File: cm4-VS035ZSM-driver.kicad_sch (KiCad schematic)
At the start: 4 parts, among them U101 USB-TYPE-C-018

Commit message: essential routing done
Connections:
- net +5V: now also Module101.77 (+5v_(Input)), Module101.79 (+5v_(Input)), Module101.81 (+5v_(Input)), Module101.83 (+5v_(Input)), Module101.85 (+5v_(Input)), Module101.87 (+5v_(Input))
- net GND: now also Module101.1 (GND), Module101.13 (GND), Module101.14 (GND), Module101.2 (GND), Module101.22 (GND), Module101.23 (GND), Module101.32 (GND), Module101.33 (GND), Module101.42 (GND), Module101.43 (GND), Module101.52 (GND), Module101.53 (GND), Module101.59 (GND), Module101.60 (GND), Module101.65 (GND), Module101.66 (GND), Module101.7 (GND), Module101.71 (GND), Module101.74 (GND), Module101.8 (GND), Module101.98 (GND)
- net +3V3: now reaches Module101.84 (+3.3v_(Output))
- net +3V3: now also Module101.86 (+3.3v_(Output))
- net +1V8: now reaches Module101.88 (+1.8v_(Output))
- net +1V8: now also Module101.90 (+1.8v_(Output))
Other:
- moved on the sheet: R101, R102, U101

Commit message: more routing
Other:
- moved on the sheet: R101, R102, U101

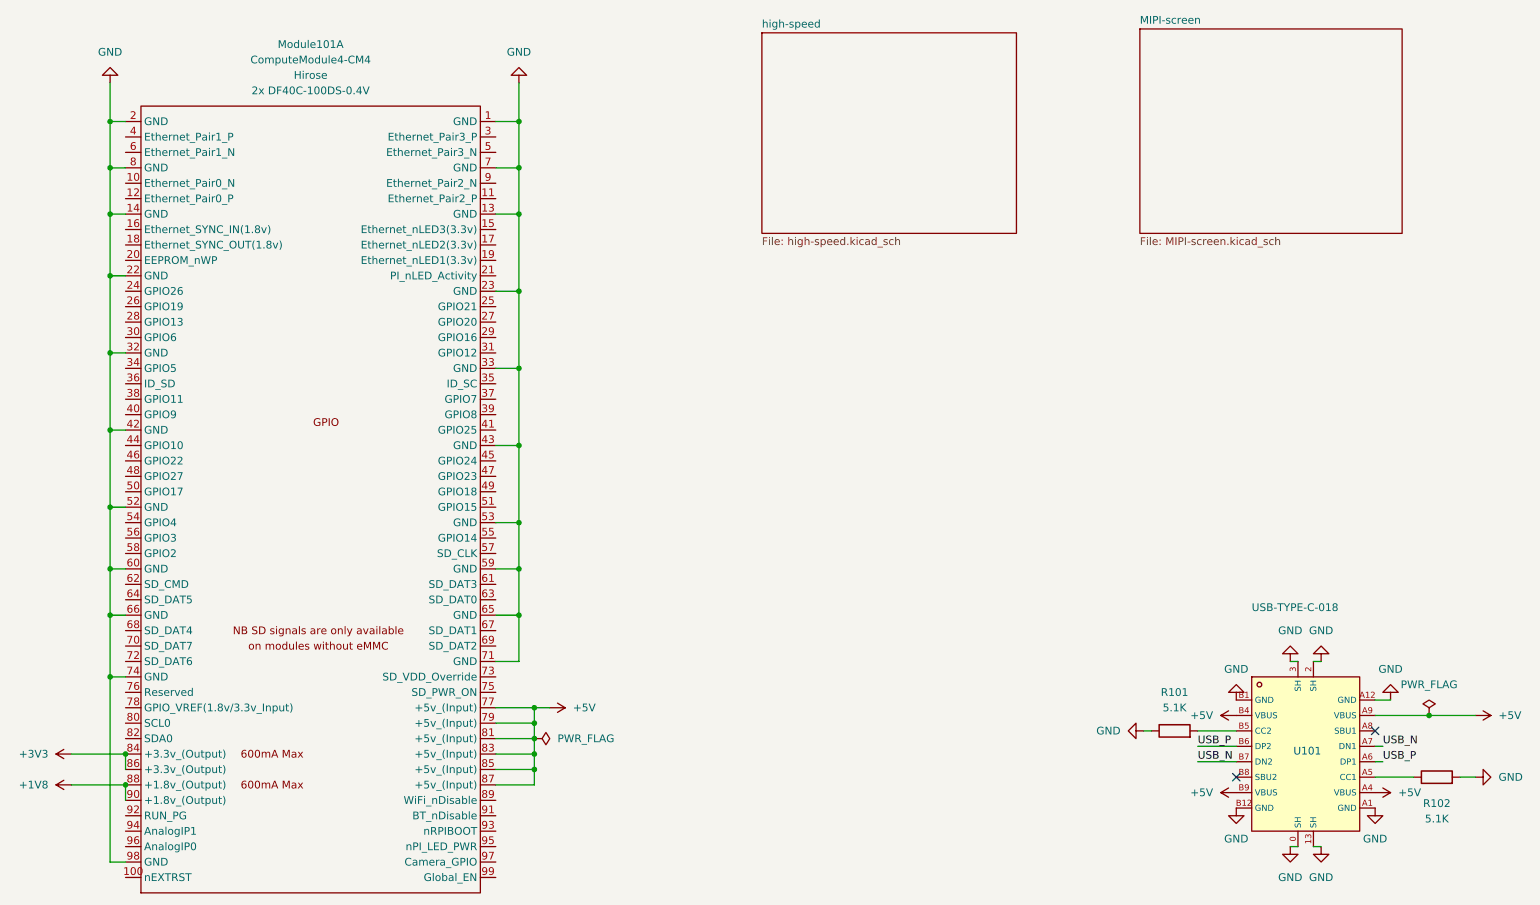
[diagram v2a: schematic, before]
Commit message: 1v8 buck and 4.7uh inductor
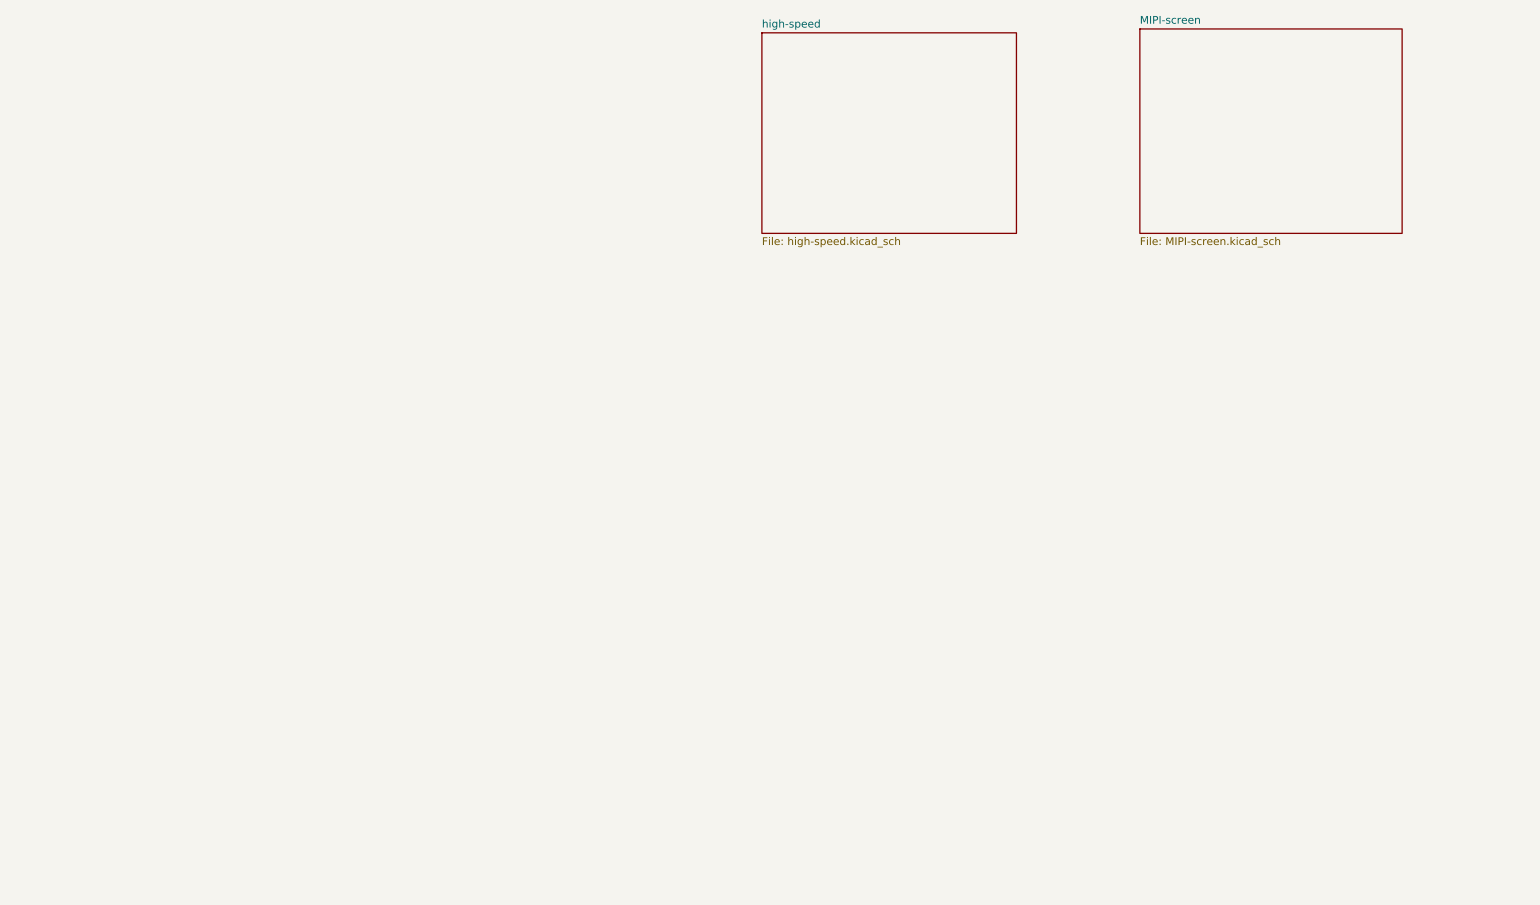
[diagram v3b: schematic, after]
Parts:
- removed Module101: ComputeModule4-CM4, CM4IO:Raspberry-Pi-4-Compute-Module, symbol CM4IO:ComputeModule4-CM4
- removed R101, R102: 5.1K, Resistor_SMD:R_0402_1005Metric, symbol Device:R
- removed U101: USB-TYPE-C-018, footprint:USB-C_SMD-TYPE-C-31-M-12, symbol USB-TYPE-C-018:USB-TYPE-C-018
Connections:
- no-connect marks 2 -> 0

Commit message: init layout
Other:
- added sheet References (references.kicad_sch)
- sheet MIPI-screen ports: added {LED_PWR}; removed none
- sheet high-speed ports: added {LED_PWR}; removed none
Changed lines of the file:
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@@
 	(generator_version "9.0")
 	(paper "A4")
+	(bus
+		(pts
+			(xy 210.82 35.56) (xy 214.63 35.56)
+		)
+		(stroke
+			(width 0)
+			(type default)
+		)
+	)
 	(sheet
-		(at 151.765 22.225)
-		(size 41.91 33.02)
+		(at 168.91 21.59)
+		(size 41.91 20.574)
 		(exclude_from_sim no)
 		(in_bom yes)
@@
 		)
 		(property "Sheetname" "high-speed"
-			(at 151.765 21.5134 0)
+			(at 168.91 20.8784 0)
 			(effects
 				(font
@@
 		)
 		(property "Sheetfile" "high-speed.kicad_sch"
-			(at 151.765 55.8296 0)
+			(at 168.91 42.7486 0)
 			(effects
 				(font
@@
 				)
 				(justify left top)
+			)
+		)
+		(pin "{LED_PWR}" input
+			(at 210.82 35.56 0)
+			(effects
+				(font
+					(size 1.27 1.27)
+				)
+				(justify right)
 			)
 		)
@@
 	)
 	(sheet
-		(at 213.995 21.59)
-		(size 43.18 33.655)
+		(at 213.36 62.23)
+		(size 44.45 38.1)
+		(exclude_from_sim no)
+		(in_bom yes)
+		(on_board yes)
+		(dnp no)
+		(fields_autoplaced yes)
+		(stroke
+			(width 0.1524)
+			(type solid)
+		)
+		(fill
+			(color 0 0 0 0.0000)
+		)
+		(property "Sheetname" "References"
+			(at 213.36 61.5184 0)
+			(effects
+				(font
+					(size 1.27 1.27)
+				)
+				(justify left bottom)
+			)
+		)
+		(property "Sheetfile" "references.kicad_sch"
+			(at 213.36 100.9146 0)
+			(effects
+				(font
+					(size 1.27 1.27)
+				)
+				(justify left top)
+			)
+		)
+		(instances
+			(project "cm4-VS035ZSM-driver"
+				(path "/9e206693-3fee-4fd4-91e0-40fbbe689518"
+					(page "4")
+				)
+			)
+		)
+	)
+	(sheet
+		(at 214.503 21.971)
+		(size 26.543 20.193)
 		(exclude_from_sim no)
 		(in_bom yes)
@@
 		)
 		(property "Sheetname" "MIPI-screen"
-			(at 213.995 20.8784 0)
+			(at 214.503 21.2594 0)
 			(effects
 				(font
@@
 		)
 		(property "Sheetfile" "MIPI-screen.kicad_sch"
-			(at 213.995 55.8296 0)
+			(at 214.503 42.7486 0)
 			(effects
 				(font
@@
 			)
 		)
+		(pin "{LED_PWR}" input
+			(at 214.503 35.56 180)
+			(effects
+				(font
+					(size 1.27 1.27)
+				)
+				(justify left)
+			)
+		)

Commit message: ok imma try kicad 10
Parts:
- added C212, C214, C220, C221, C222, C223: 4.7uF/16V, Capacitor_SMD:C_0603_1608Metric, symbol Device:C
- added C213, C215: 2.2uF/50V, Capacitor_SMD:C_0805_2012Metric, symbol Device:C
- added C216: 10uF/25V, Capacitor_SMD:C_0603_1608Metric, symbol Device:C
- added D403: B5817WS_C7420329, footprints:SOD-323_L1.7-W1.3-LS2.5-FD, symbol B5817WS_C7420329:B5817WS_C7420329
- added H1, H2, H3: MountingHole_Pad, MountingHole:MountingHole_3.2mm_M3_DIN965_Pad_TopBottom, symbol Mechanical:MountingHole_Pad
- added J1: Conn_01x22, footprints:CON22_1X22_DRB_XF2C_TYC, symbol XF2M-2215-1A:XF2M-2215-1A
- added J3: 245863050104829+, footprints:245863050104829_missing pads, symbol 245863050104829+:245863050104829+_missing_gnd
- added L204, L206, L207: 4.7uH, footprints:IND-SMD_L2.5-W2.0_SPH252012, symbol Device:L
- added R206: 5.1Ω/1%, Resistor_SMD:R_0805_2012Metric, symbol Device:R
- added R209: 100KΩ/1%, Resistor_SMD:R_0402_1005Metric, symbol Device:R
- added R3: 2.2kΩ, Resistor_SMD:R_0402_1005Metric, symbol Device:R
- added R4: 2.7kΩ, Resistor_SMD:R_0603_1608Metric, symbol Device:R
- added TP201: Test-1V8, TestPoint:TestPoint_THTPad_D2.0mm_Drill1.0mm, symbol Connector:TestPoint
- added U1: PZ254-2-08-WS, footprints:HDR-SMD_16P-P2.54-H-M-R2-C8-W12.0-N, symbol PZ254-2-08-WS:PZ254-2-08-WS
- added U2, U3: KF1027B-04P-G00-DFT-01B, footprints:SW-SMD_KF1027B-04P-G00-DFT-01B, symbol KF1027B-04P-G00-DFT-01B:KF1027B-04P-G00-DFT-01B
- added U202: TPS65132WRVCR_C2876379, footprints:WQFN-20_L4.0-W3.0-P0.50-BL-EP, symbol TPS65132WRVCR_C2876379:TPS65132WRVCR_C2876379
- added U203: LP3320B6F, footprints:SOT-23-6_L2.9-W1.6-P0.95-LS2.8-BL, symbol LP3320B6F:LP3320B6F
- added U204: MCP1603T-180I/OS, footprints:TSOT5_MC_MCH, symbol MCP1603T_180I_OS:MCP1603T-180I_OS
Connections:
- new net: L206.1, U204.5 (LX)
- new net: C222.1, U202.14 (REG), U202.18 (REG)
- new net: C213.1, U202.10 (CFLY2)
- new net: C213.2, U202.13 (CFLY1)
- new net: D403.1 (A), L204.2, U203.1 (LX)
- new net +1V8: J3.2, J3.4, J3.8, U3.4 (A4)
- new net +3V3: J1.22 (Pin_22), U1.10, U2.5 (B4), U2.6 (B3), U2.7 (B2), U2.8 (B1)
- new net +5V7: J3.3, U3.3 (A3)
- new net +5V7_EN: U1.6, U2.3 (A3), U202.5 (ENP)
- new net +5V7_OUT: C221.1, U202.15 (OUTP), U202.16 (OUTP), U3.6 (B3)
- new net +5V_IN: C214.2, C216.2, C223.1, L204.1, L207.1, U1.12, U202.4 (VIN), U203.6 (VIN), U204.1 (VIN)
- new net -5V7: J3.7, U3.2 (A2)
- new net -5V7_EN: U1.4, U2.2 (A2), U202.6 (ENN)
- new net -5V7_OUT: C220.1, U202.9 (OUTN), U3.7 (B2)
- new net 1V8_EN: U1.8, U2.4 (A4), U204.3 (*SHDN)
- new net 1V8_OUT: C212.1, L206.2, TP201.1, U204.4 (VFB/VOUT), U3.5 (B4)
- new net BL_DRV_EN: U1.2, U2.1 (A1)
- new net DSI0_CLK.N: J1.8 (Pin_8), J3.18
- new net DSI0_CLK.P: J1.9 (Pin_9), J3.20
- new net DSI0_DATA.0_N: J1.2 (Pin_2), J3.11
- new net DSI0_DATA.0_P: J1.3 (Pin_3), J3.13
- new net DSI0_DATA.1_N: J1.5 (Pin_5), J3.17
- new net DSI0_DATA.1_P: J1.6 (Pin_6), J3.19
- new net DSI0_DATA.2_N: J1.12 (Pin_12), J3.24
- new net DSI0_DATA.2_P: J1.11 (Pin_11), J3.26
- new net DSI0_DATA.3_N: J1.15 (Pin_15), J3.12
- new net DSI0_DATA.3_P: J1.14 (Pin_14), J3.14
- new net GND: C212.2, C214.1, C215.2, C216.1, C220.2, C221.2, C222.2, C223.2, H1.1, H2.1, H3.1, J1.1 (Pin_1), J1.10 (Pin_10), J1.13 (Pin_13), J1.16 (Pin_16), J1.19 (Pin_19), J1.23 (Pin_23_case), J1.24 (Pin_24_case), J1.4 (Pin_4), J1.7 (Pin_7), J3.1, J3.10, J3.15, J3.16, J3.21, J3.22, J3.27, J3.28, J3.33, J3.34, J3.39, J3.40, J3.43, J3.46, J3.49, J3.5, J3.50, J3.6, J3.9, J3.MP1, J3.MP2, J3.MP3, J3.MP4, J3.MP5, J3.MP6, R206.2, R209.2, R4.2, U202.1 (PGND), U202.11 (PGND), U202.12 (PGND), U202.17 (AGND), U202.2 (PGND), U202.21 (EP), U202.3 (AGND), U203.2 (GND), U204.2 (GND)
- new net LCD_CONNECTOR_PWM: J3.48, U1.5
- new net LCD_RESET_1V8: J3.42, R3.2, R4.1, U1.1
- new net LCD_RESET_3V3: J1.17 (Pin_17), R3.1, U1.3
- new net LED_PWM: J1.18 (Pin_18), R209.1, U1.9, U203.4 (EN)
- new net LED_PWR.A_IN: J3.41, U3.1 (A1)
- new net LED_PWR.A_OUT: C215.1, D403.2 (K), U1.14, U3.8 (B1)
- new net LED_PWR.K: J3.45, J3.47, R206.1, U1.16, U203.3 (FB)
- new net SCL_3V3: J1.20 (Pin_20), U1.13, U202.8 (SCL)
- new net SDA_3V3: J1.21 (Pin_21), U1.15, U202.7 (SDA)
- new net SW: L207.2, U202.19 (SW), U202.20 (SW)
- new net TE: J3.44, U1.11
- no-connect marks 0 -> 11
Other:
- removed sheet MIPI-screen
- removed sheet References
- removed sheet high-speed
- note added: "1V8 Buck"
- note added: "Broken out for testing"
- note added: "Display Mezzanine"
- note added: "Interfacing"
- note added: "LCD Bias"
- note added: "LED driver"
- note added: "LED goes between here FB is used to sense drop in voltage"
- note added: "Need 5V input, all the chips does accept 5v in"
- note added: "PWM controlled"
- note added: "Pi ribbon cable"
- note added: "Positive 5.7V and negative 5.7V"
- note added: "input"
- note added: "manual enable for power"
- note added: "manual voltage rail control (off by default)"
- note added: "output"

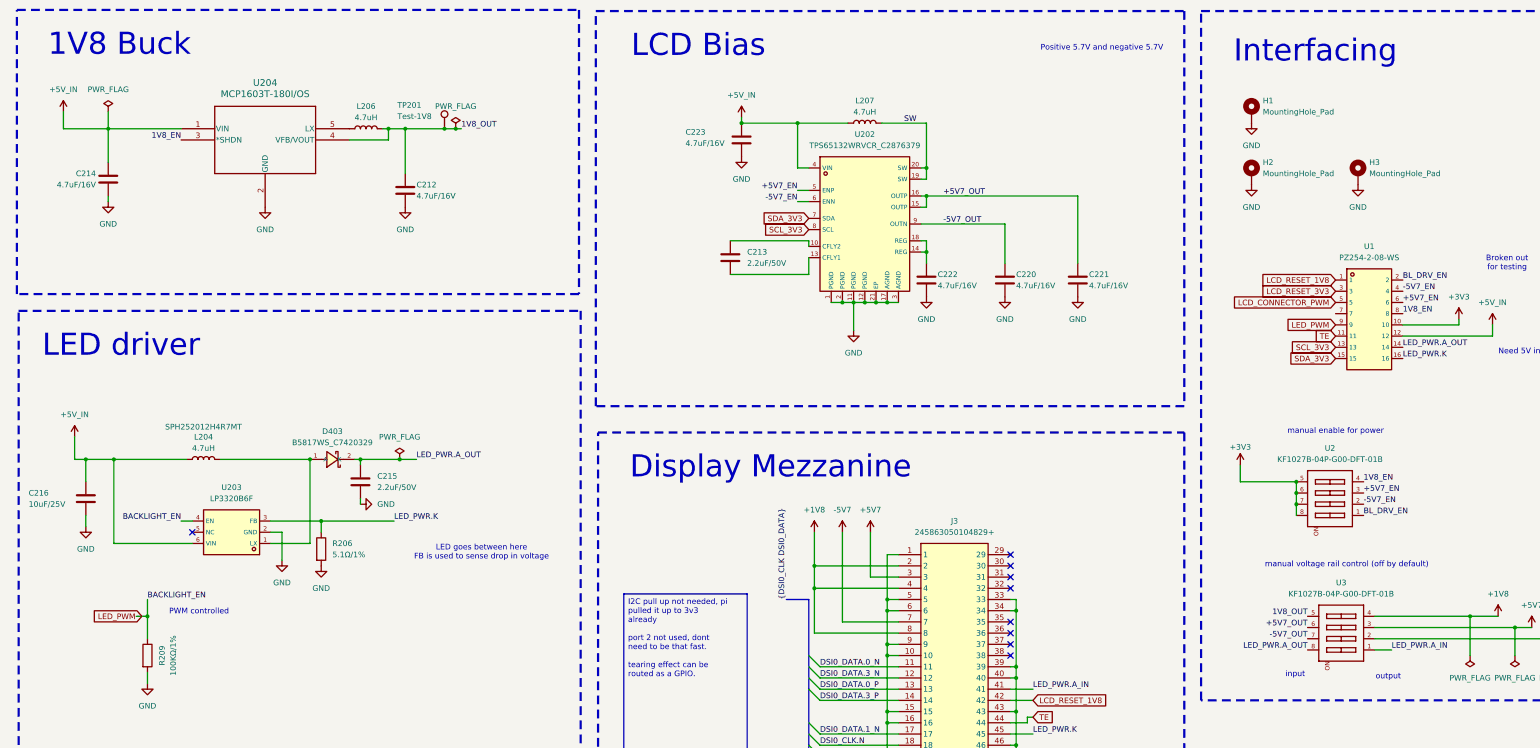
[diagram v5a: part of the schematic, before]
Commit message: finalized board before rounding corners
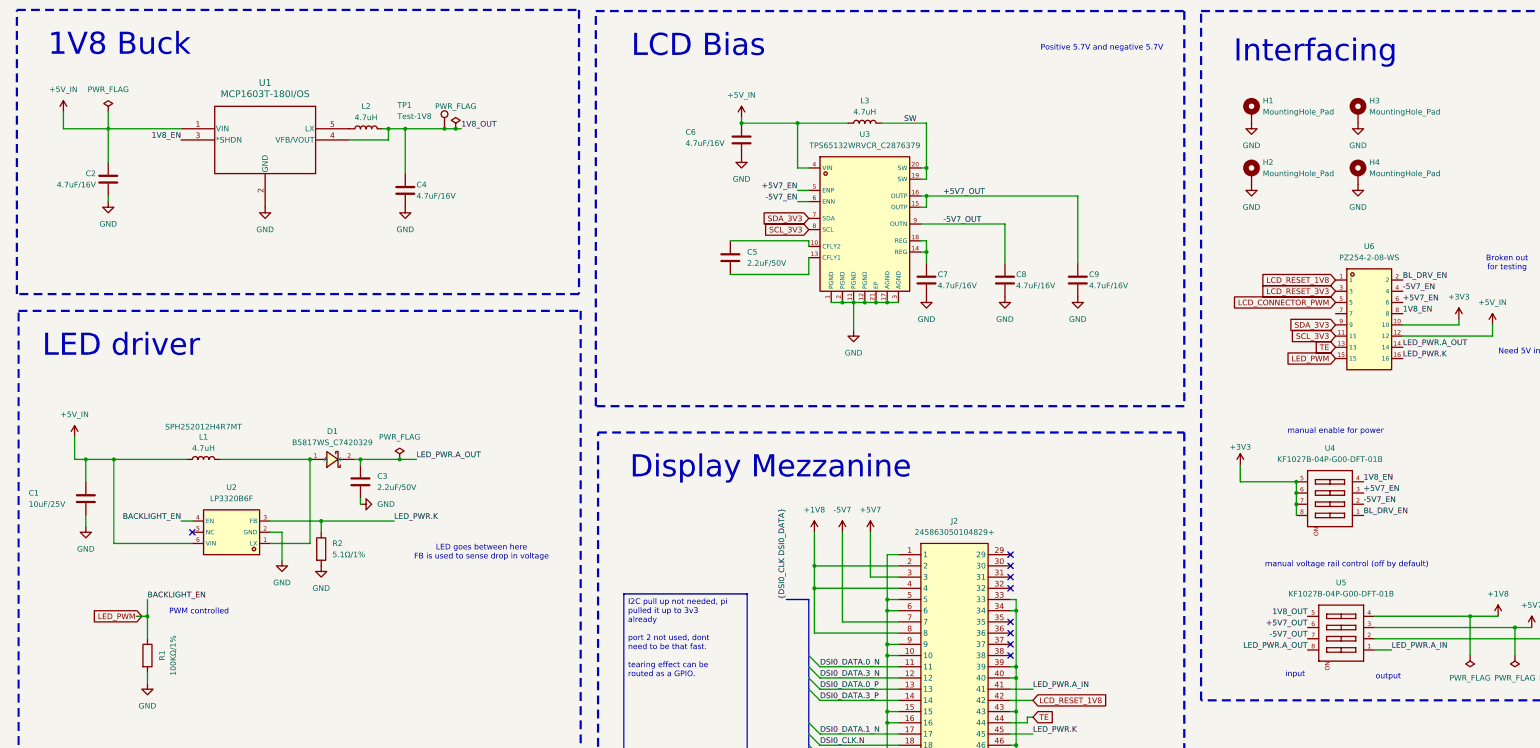
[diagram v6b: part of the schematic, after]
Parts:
- added H3: MountingHole_Pad, MountingHole:MountingHole_3.2mm_M3_DIN965_Pad_TopBottom, symbol Mechanical:MountingHole_Pad
- renumbered C216 to C1, C214 to C2, C215 to C3, C212 to C4, C213 to C5, C223 to C6, C222 to C7, C220 to C8, C221 to C9, D403 to D1, H3 to H4, J3 to J2, L204 to L1, L206 to L2, L207 to L3, R209 to R1, R206 to R2, TP201 to TP1, U204 to U1, U203 to U2, U202 to U3, U2 to U4, U3 to U5, U1 to U6
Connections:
- net GND: now also H3.1
- net LED_PWM: now also U6.15; no longer U6.9
- net SCL_3V3: now also U6.11; no longer U6.13
- net SDA_3V3: now also U6.9; no longer U6.15
- net TE: now also U6.13; no longer U6.11

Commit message: done with v2
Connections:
- no-connect marks 11 -> 12
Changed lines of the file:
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@@
+	)
+	(no_connect
+		(at 313.69 83.82)
 	)
 	(no_connect

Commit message: swap J2 connector to full-pads variant and use vias for routing
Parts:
- removed J2: 245863050104829+, footprints:245863050104829_missing pads, symbol 245863050104829+:245863050104829+_missing_gnd
- added J2: 245863050104829+, 245863050104829, symbol 245863050104829+:245863050104829+
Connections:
- net +1V8: now also J2.2, J2.4, J2.8
- net +5V7: now also J2.3
- net -5V7: now also J2.7
- net DSI0_CLK.N: now also J2.18
- net DSI0_CLK.P: now also J2.20
- net DSI0_DATA.0_N: now also J2.11
- net DSI0_DATA.0_P: now also J2.13
- net DSI0_DATA.1_N: now also J2.17
- net DSI0_DATA.1_P: now also J2.19
- net DSI0_DATA.2_N: now also J2.24
- net DSI0_DATA.2_P: now also J2.26
- net DSI0_DATA.3_N: now also J2.12
- net DSI0_DATA.3_P: now also J2.14
- net GND: now also J2.1, J2.10, J2.15, J2.16, J2.21, J2.22, J2.27, J2.28, J2.33, J2.34, J2.39, J2.40, J2.43, J2.46, J2.49, J2.5, J2.50, J2.6, J2.9, J2.MP1, J2.MP2, J2.MP3, J2.MP4, J2.MP5, J2.MP6
- net LCD_CONNECTOR_PWM: now also J2.48
- net LCD_RESET_1V8: now also J2.42
- net LED_PWR.A_IN: now also J2.41
- net LED_PWR.K: now also J2.45, J2.47
- net TE: now also J2.44
